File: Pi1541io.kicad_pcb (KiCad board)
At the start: 2 copper layers, 65 x 56 mm, 54 parts, among them J1 IEC1, J10 SDA, J11 SCL, J12 I2C, J13 SDA, J14 SDA, J15 SDA, J2 IEC2, J3 IEC3, J4 ExtSpkr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

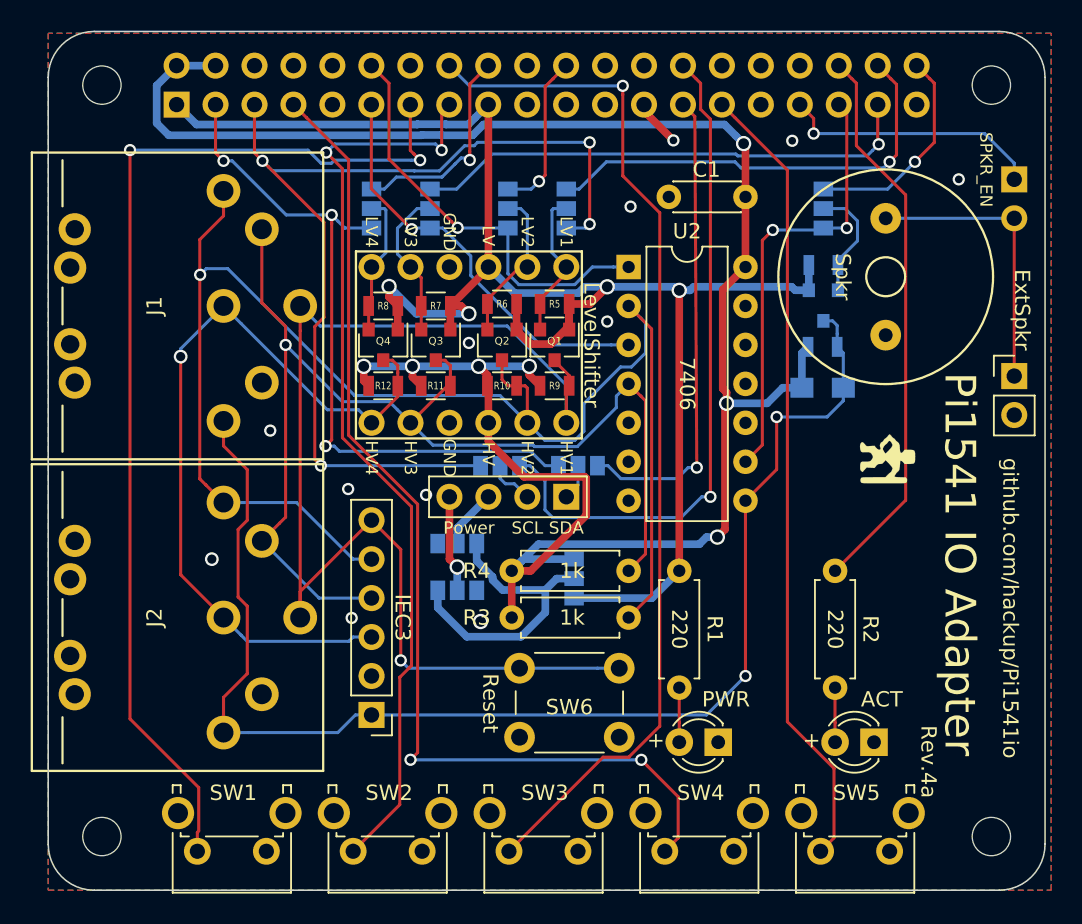
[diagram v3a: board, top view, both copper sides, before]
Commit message: Relocated reset button.
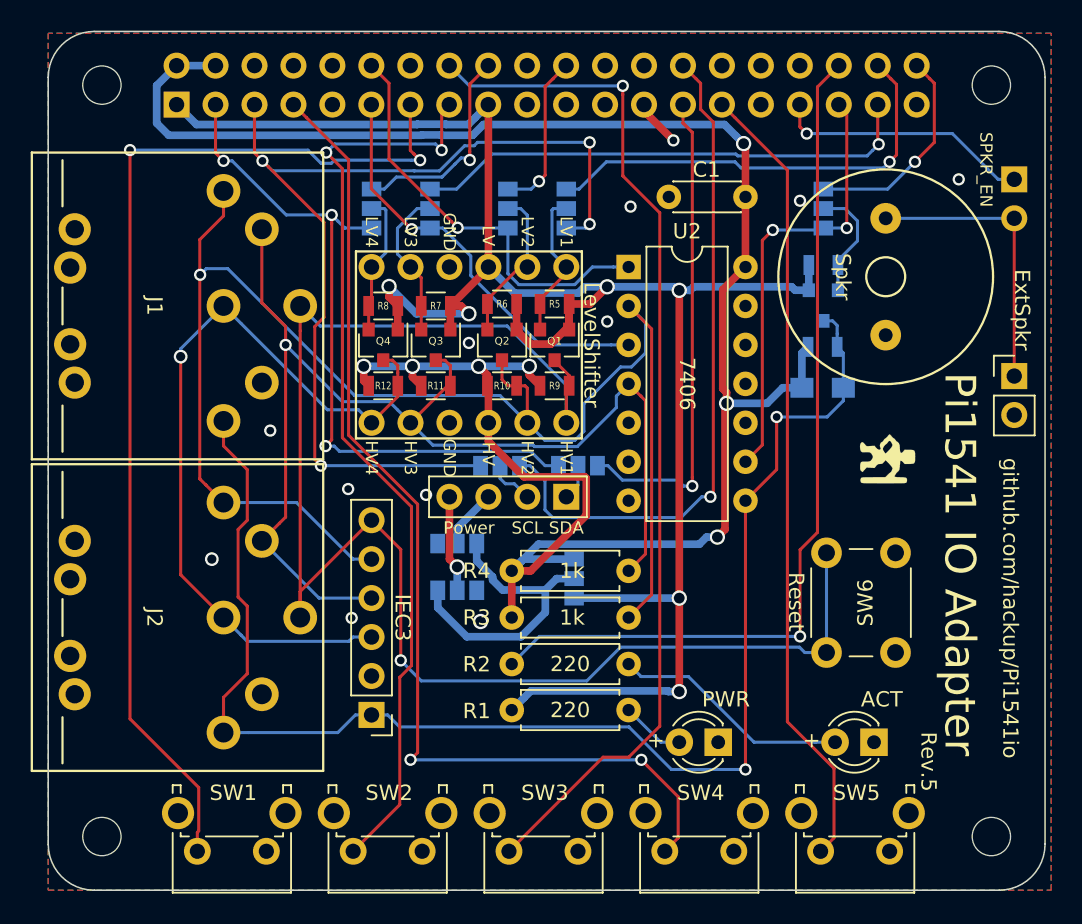
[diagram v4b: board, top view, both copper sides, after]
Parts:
- moved R2 21.9 mm to (136.4, 100.5), turned to 0 degrees
- moved SW6 20.0 mm to (156.9, 99.7), turned to 90 degrees
- moved R1 14.2 mm to (136.4, 103.5), turned to 0 degrees
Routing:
- net RESET: track 79.6 -> 101.0 mm
- net /GPIO16: track 36.7 -> 57.8 mm, vias 0 -> 1
- net +3V3: track 109.2 -> 127.8 mm, vias 4 -> 6
- net Net-(D2-Pad2): track 3.56 -> 15.6 mm
- net SRQ: track 86.3 -> 92.8 mm
- net I2C0_SDA: track 31.1 -> 31.9 mm
- net Net-(D1-Pad2): track 3.56 -> 4.17 mm
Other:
- board text added: "Rev.5"
- board text removed: "Rev.4a"

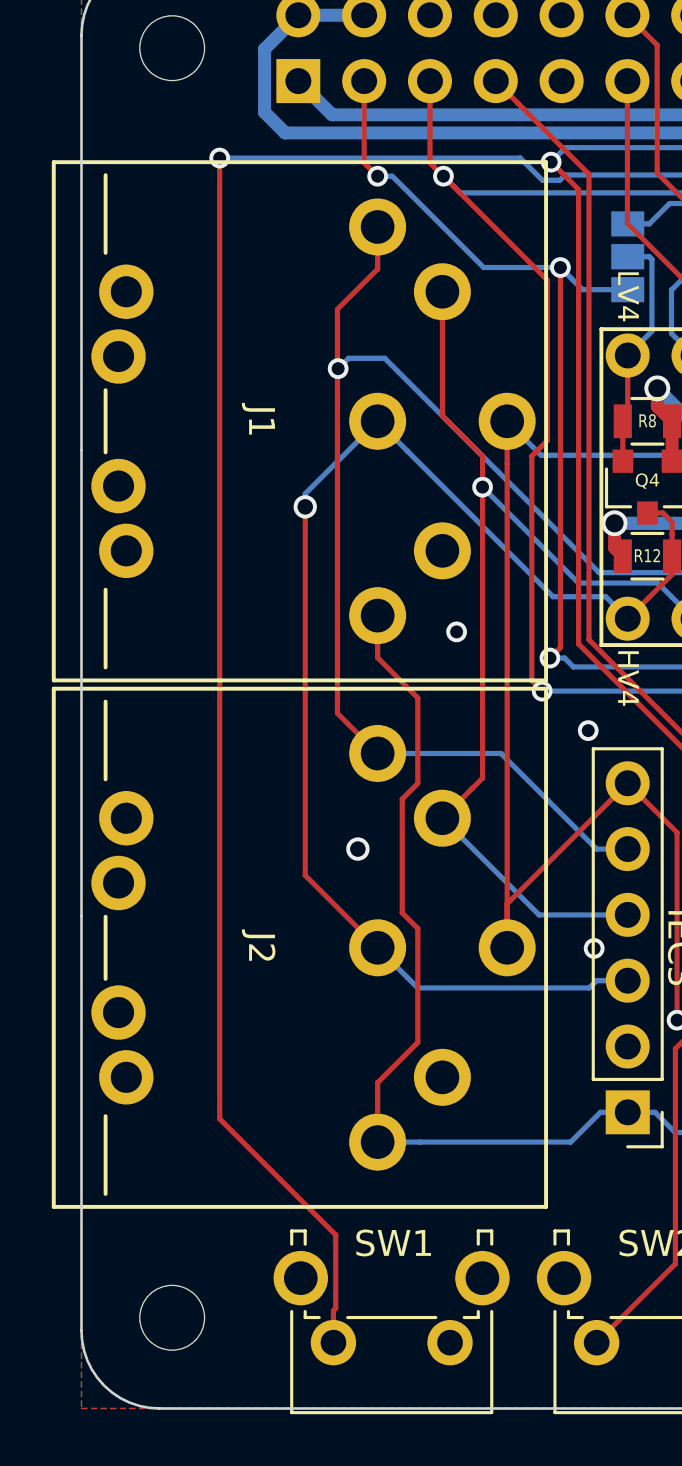
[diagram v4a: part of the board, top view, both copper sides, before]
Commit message: Added ziptie holes.
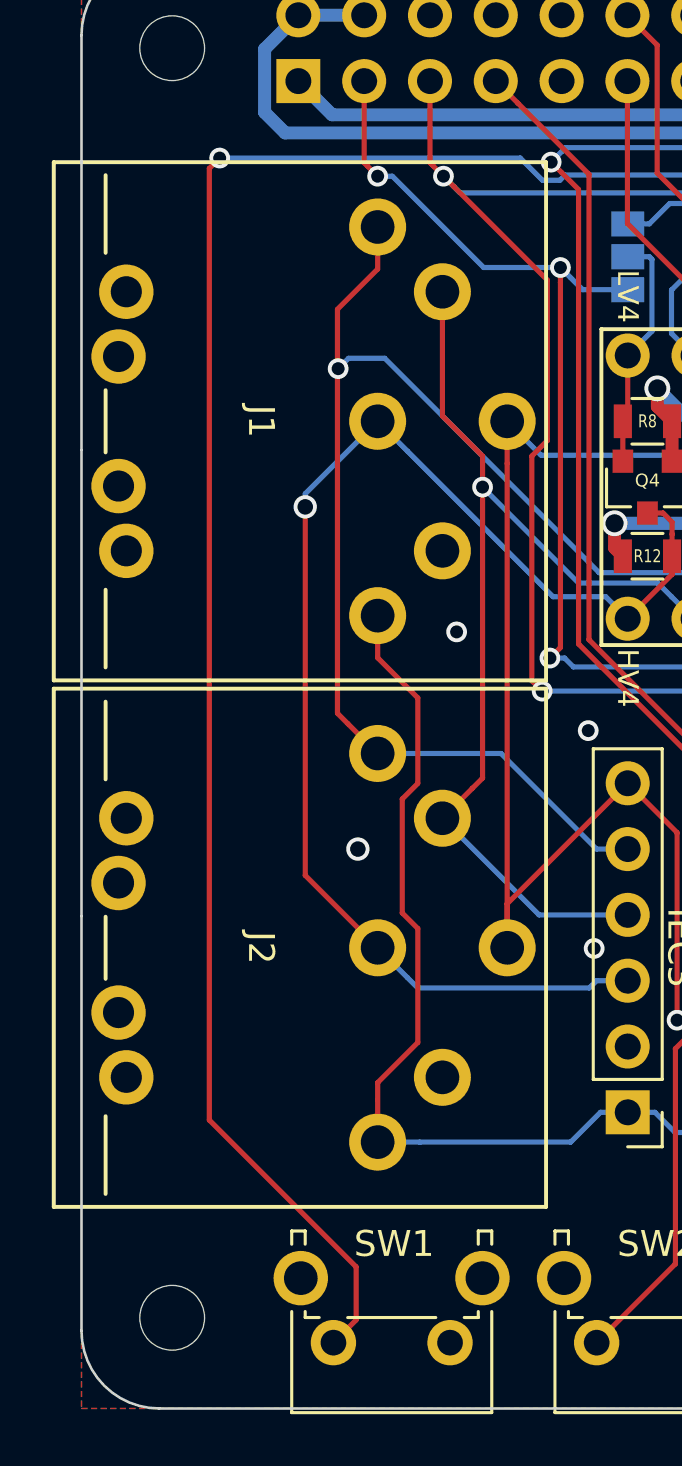
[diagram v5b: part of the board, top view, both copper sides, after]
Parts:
- added MK5: ZipTie, DIN-Connector:ZipTie_2.7mm, F.Cu at (112.8, 95.0)
- added MK6: ZipTie, DIN-Connector:ZipTie_2.7mm, F.Cu at (112.8, 99.8)
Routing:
- net /GPIO27(GEN2): track 70.9 -> 71.8 mm
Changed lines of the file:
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@@
     (tracks 583)
     (zones 0)
-    (modules 54)
+    (modules 56)
     (nets 50)
   )
@@
     (pad 6 thru_hole circle (at 0 5 90) (size 2.2 2.2) (drill 1.3) (layers *.Cu *.Mask)
       (net 21 RESET) (solder_mask_margin 0.15) (clearance 0.3))
+  )
+  (module DIN-Connector:ZipTie_2.7mm (layer F.Cu)
+    (at 112.786001 95.016)
+    (descr "Mounting Hole 2.7mm, no annular")
+    (tags "mounting hole 2.7mm no annular")
+    (attr virtual)
+    (fp_text reference MK5 (at 0 -1.778) (layer F.SilkS) hide
+      (effects (font (size 1 1) (thickness 0.15)))
+    )
+    (fp_text value ZipTie (at 0 1.905) (layer F.Fab)
+      (effects (font (size 1 1) (thickness 0.15)))
+    )
+    (fp_arc (start -1.143 0) (end -1.143 -1.016) (angle -180) (layer F.CrtYd) (width 0.07))
+    (fp_arc (start 1.143 0) (end 1.143 1.016) (angle -180) (layer F.CrtYd) (width 0.07))
+    (fp_line (start -1.143 1.016) (end 1.143 1.016) (layer F.CrtYd) (width 0.07))
+    (fp_line (start -1.143 -1.016) (end 1.143 -1.016) (layer F.CrtYd) (width 0.07))
+    (fp_arc (start -0.889 0) (end -0.889 -0.762) (angle -180) (layer Cmts.User) (width 0.15))
+    (fp_arc (start 0.889 0) (end 0.889 0.762) (angle -180) (layer Cmts.User) (width 0.15))
+    (fp_line (start -0.889 0.762) (end 0.889 0.762) (layer Cmts.User) (width 0.15))
+    (fp_line (start -0.889 -0.762) (end 0.889 -0.762) (layer Cmts.User) (width 0.15))
+    (fp_text user %R (at 0.3 0) (layer F.Fab)
+      (effects (font (size 1 1) (thickness 0.15)))
+    )
+    (pad "" np_thru_hole oval (at 0 0) (size 2.7 1.1) (drill oval 2.7 1.1) (layers *.Cu *.Mask))
+  )
+  (module DIN-Connector:ZipTie_2.7mm (layer F.Cu)
+    (at 112.786001 99.816)
+    (descr "Mounting Hole 2.7mm, no annular")
+    (tags "mounting hole 2.7mm no annular")
+    (attr virtual)
+    (fp_text reference MK6 (at 0 -1.778) (layer F.SilkS) hide
+      (effects (font (size 1 1) (thickness 0.15)))
+    )
+    (fp_text value ZipTie (at 0 1.905) (layer F.Fab)
+      (effects (font (size 1 1) (thickness 0.15)))
+    )
+    (fp_text user %R (at 0.3 0) (layer F.Fab)
+      (effects (font (size 1 1) (thickness 0.15)))
+    )
+    (fp_line (start -0.889 -0.762) (end 0.889 -0.762) (layer Cmts.User) (width 0.15))
+    (fp_line (start -0.889 0.762) (end 0.889 0.762) (layer Cmts.User) (width 0.15))
+    (fp_arc (start 0.889 0) (end 0.889 0.762) (angle -180) (layer Cmts.User) (width 0.15))
+    (fp_arc (start -0.889 0) (end -0.889 -0.762) (angle -180) (layer Cmts.User) (width 0.15))
+    (fp_line (start -1.143 -1.016) (end 1.143 -1.016) (layer F.CrtYd) (width 0.07))
+    (fp_line (start -1.143 1.016) (end 1.143 1.016) (layer F.CrtYd) (width 0.07))
+    (fp_arc (start 1.143 0) (end 1.143 1.016) (angle -180) (layer F.CrtYd) (width 0.07))
+    (fp_arc (start -1.143 0) (end -1.143 -1.016) (angle -180) (layer F.CrtYd) (width 0.07))
+    (pad "" np_thru_hole oval (at 0 0) (size 2.7 1.1) (drill oval 2.7 1.1) (layers *.Cu *.Mask))
   )
   (gr_line (start 137.5 103.391) (end 142.847 103.391) (layer B.SilkS) (width 0.1))
@@
   (segment (start 125.732085 67.567085) (end 122.986999 64.821999) (width 0.2) (layer F.Cu) (net 6))
   (segment (start 130.234012 106.227988) (end 130.234012 90.03131) (width 0.2) (layer F.Cu) (net 6))
-  (segment (start 115.961001 111.334563) (end 115.961001 108.506001) (width 0.2) (layer F.Cu) (net 9))
-  (segment (start 115.871 112.662) (end 115.871 111.424564) (width 0.2) (layer F.Cu) (net 9))
-  (segment (start 115.871 111.424564) (end 115.961001 111.334563) (width 0.2) (layer F.Cu) (net 9))
   (via (at 111.481 66.942) (size 0.8) (drill 0.5) (layers F.Cu B.Cu) (net 9))
-  (segment (start 115.961001 108.506001) (end 111.481 104.026) (width 0.2) (layer F.Cu) (net 9))
-  (segment (start 111.481 104.026) (end 111.481 66.942) (width 0.2) (layer F.Cu) (net 9))
   (segment (start 129.757 66.955942) (end 129.997963 67.196905) (width 0.2) (layer F.Cu) (net 9))
   (segment (start 129.997963 67.196905) (end 130.397962 67.596904) (width 0.2) (layer F.Cu) (net 9))
@@
   (segment (start 129.832277 67.596904) (end 130.397962 67.596904) (width 0.2) (layer B.Cu) (net 9))
   (segment (start 124.812356 67.596904) (end 129.832277 67.596904) (width 0.2) (layer B.Cu) (net 9))
+  (segment (start 111.081001 67.341999) (end 111.081001 104.070501) (width 0.2) (layer F.Cu) (net 9))
+  (segment (start 111.481 66.942) (end 111.081001 67.341999) (width 0.2) (layer F.Cu) (net 9))
+  (segment (start 116.745999 111.787001) (end 115.871 112.662) (width 0.2) (layer F.Cu) (net 9))
+  (segment (start 116.745999 109.735499) (end 116.745999 111.787001) (width 0.2) (layer F.Cu) (net 9))
+  (segment (start 111.081001 104.070501) (end 116.745999 109.735499) (width 0.2) (layer F.Cu) (net 9))
   (via (at 131.801 66.942) (size 0.8) (drill 0.5) (layers F.Cu B.Cu) (net 10))
   (segment (start 131.801 64.468) (end 132.297 63.972) (width 0.2) (layer F.Cu) (net 10))
@@
   (segment (start 117.577 77.102) (end 114.783 79.896) (width 0.2) (layer B.Cu) (net 20) (status 10))
   (segment (start 114.783 79.896) (end 114.783 80.404) (width 0.2) (layer B.Cu) (net 20))
-  (segment (start 114.783 94.628) (end 117.577 97.422) (width 0.2) (layer F.Cu) (net 20) (status 20))
-  (segment (start 114.783 80.404) (end 114.783 94.628) (width 0.2) (layer F.Cu) (net 20))
   (segment (start 118.726999 78.251999) (end 117.577 77.102) (width 0.2) (layer B.Cu) (net 20))
   (segment (start 124.347001 83.872001) (end 118.726999 78.251999) (width 0.2) (layer B.Cu) (net 20))
@@
   (segment (start 126.026919 98.692) (end 125.746918 98.972001) (width 0.2) (layer B.Cu) (net 20))
   (segment (start 127.229 98.692) (end 126.026919 98.692) (width 0.2) (layer B.Cu) (net 20))
+  (segment (start 114.783 94.628) (end 114.783 80.404) (width 0.2) (layer F.Cu) (net 20))
+  (segment (start 117.577 97.422) (end 114.783 94.628) (width 0.2) (layer F.Cu) (net 20))
   (segment (start 122.577 78.728345) (end 122.577 97.422) (width 0.2) (layer F.Cu) (net 21) (status 20))
   (segment (start 122.577 77.102) (end 122.577 78.728345) (width 0.2) (layer F.Cu) (net 21) (status 10))

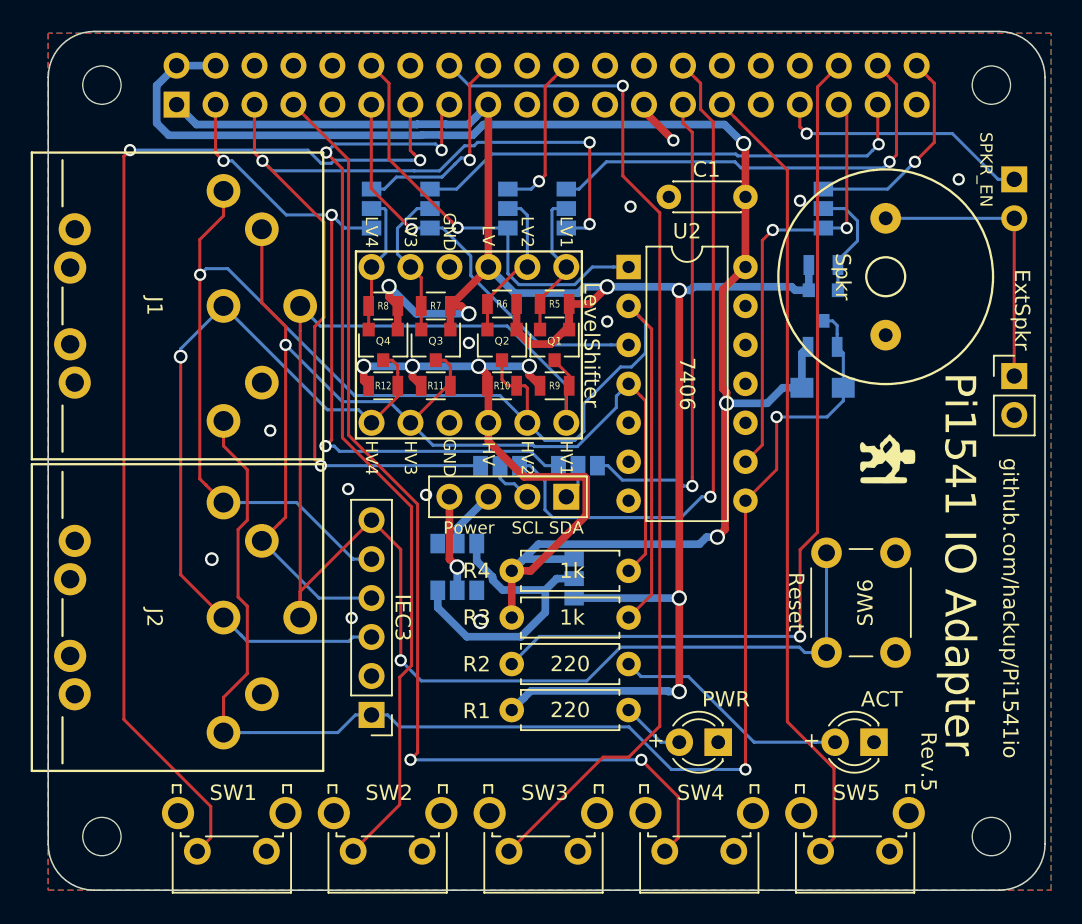
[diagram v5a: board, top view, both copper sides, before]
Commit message: Moved LEDs, texts, reset button, and speaker.
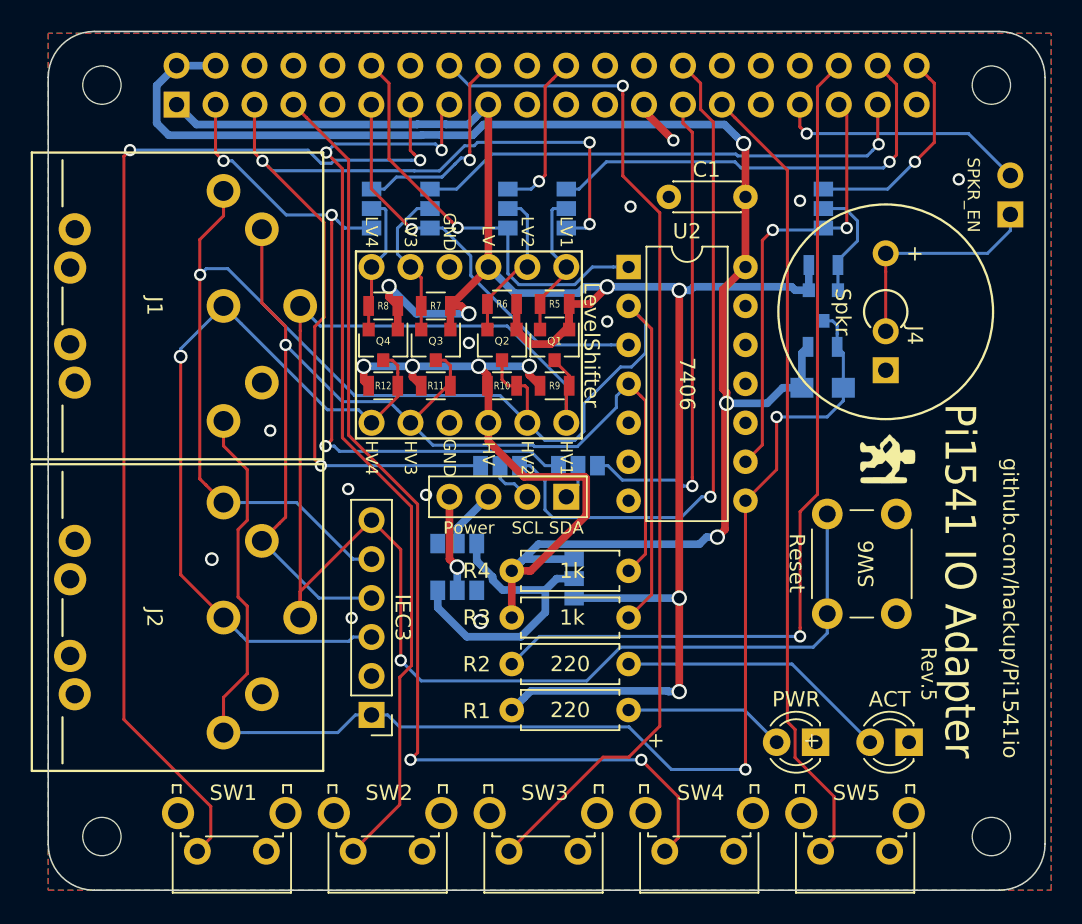
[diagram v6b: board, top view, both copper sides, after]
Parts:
- removed JP1: SPKR_EN, Pin_Headers:Pin_Header_Straight_1x02_Pitch2.54mm
- added SW7: SPKR_EN, Pin_Headers:Pin_Header_Straight_2x01_Pitch2.54mm, F.Cu at (168.9, 71.1)
- J4: footprint Pin_Headers:Pin_Header_Straight_1x02_Pitch2.54mm -> Pin_Headers:Pin_Header_Straight_1x01_Pitch2.54mm
- moved J4 8.88 mm to (160.8, 78.8)
- moved D1 6.35 mm to (156.2, 105.5)
- moved SW6 2.53 mm to (156.9, 97.2)
- moved D2 2.29 mm to (162.3, 105.5)
- moved LS1 2.29 mm to (160.8, 77.5)
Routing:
- net Net-(D1-Pad2): track 4.17 -> 10.5 mm
- net Net-(J4-Pad1): track 18.7 -> 14.9 mm
- net Net-(D2-Pad2): track 15.6 -> 17.9 mm
- net RESET: track 101.0 -> 102.5 mm
